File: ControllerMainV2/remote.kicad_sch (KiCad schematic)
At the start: 26 parts, among them IC22 1462039-4, IC23 1462039-4, IC24 1462039-4, IC25 1462039-4, J28 Conn_01x03, J29 Conn_01x03, J31 Conn_01x03, Q1 2N7002, Q2 2N7002, Q3 2N7002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

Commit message: Added libs
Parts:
- removed J28, J29, J31: Conn_01x03, symbol Connector_Generic:Conn_01x03
- removed J30: (no value), symbol Connector_Generic:Conn_01x03

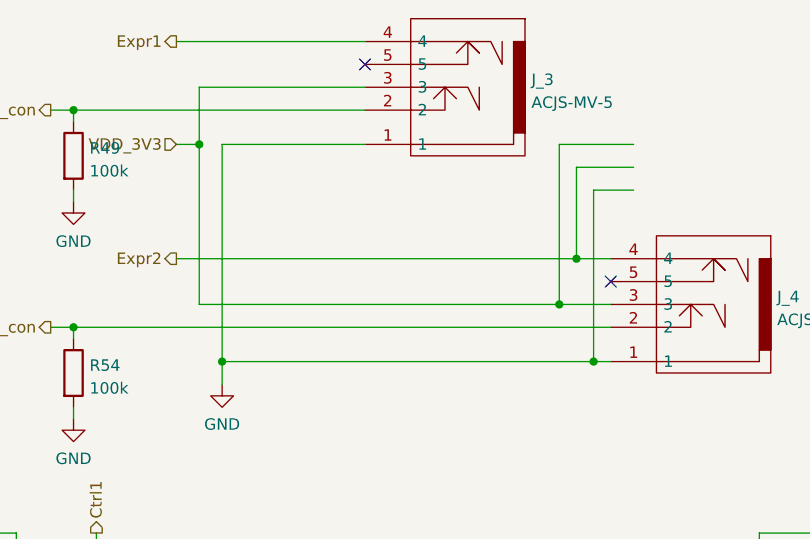
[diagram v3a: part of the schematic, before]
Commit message: 3D models and fixed pcbs
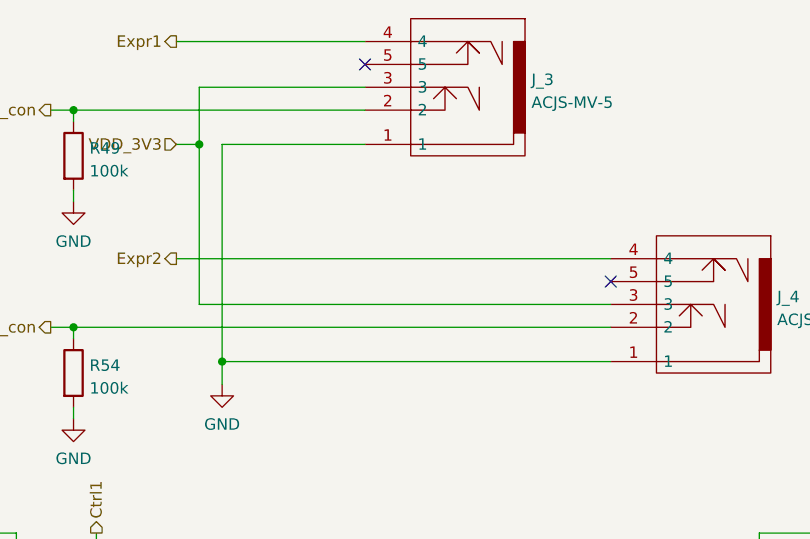
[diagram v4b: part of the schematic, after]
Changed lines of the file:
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@@
   (junction (at 111.76 80.01) (diameter 0) (color 0 0 0 0)
   )
-  (junction (at 167.005 58.42) (diameter 0) (color 0 0 0 0)
-  )
   (junction (at 102.87 130.81) (diameter 0) (color 0 0 0 0)
   )
@@
   (junction (at 123.19 34.29) (diameter 0) (color 0 0 0 0)
   )
-  (junction (at 163.195 52.07) (diameter 0) (color 0 0 0 0)
-  )
   (junction (at 240.03 90.17) (diameter 0) (color 0 0 0 0)
-  )
-  (junction (at 165.1 46.99) (diameter 0) (color 0 0 0 0)
   )
   (junction (at 175.26 90.17) (diameter 0) (color 0 0 0 0)
@@
     (stroke (width 0) (type default) (color 0 0 0 0))
   )
-  (wire (pts (xy 123.19 52.07) (xy 163.195 52.07))
+  (wire (pts (xy 123.19 52.07) (xy 168.91 52.07))
     (stroke (width 0) (type default) (color 0 0 0 0))
   )
@@
     (stroke (width 0) (type default) (color 0 0 0 0))
   )
-  (wire (pts (xy 163.195 52.07) (xy 168.91 52.07))
-    (stroke (width 0) (type default) (color 0 0 0 0))
-  )
   (wire (pts (xy 185.42 109.22) (xy 247.65 109.22))
     (stroke (width 0) (type default) (color 0 0 0 0))
@@
     (stroke (width 0) (type default) (color 0 0 0 0))
   )
-  (wire (pts (xy 171.45 34.29) (xy 163.195 34.29))
-    (stroke (width 0) (type default) (color 0 0 0 0))
-  )
   (wire (pts (xy 67.31 95.25) (xy 67.31 109.22))
     (stroke (width 0) (type default) (color 0 0 0 0))
   )
-  (wire (pts (xy 165.1 36.83) (xy 165.1 46.99))
-    (stroke (width 0) (type default) (color 0 0 0 0))
-  )
   (wire (pts (xy 175.26 90.17) (xy 175.26 130.81))
     (stroke (width 0) (type default) (color 0 0 0 0))
@@
     (stroke (width 0) (type default) (color 0 0 0 0))
   )
-  (wire (pts (xy 171.45 36.83) (xy 165.1 36.83))
-    (stroke (width 0) (type default) (color 0 0 0 0))
-  )
   (wire (pts (xy 186.69 97.79) (xy 184.15 97.79))
     (stroke (width 0) (type default) (color 0 0 0 0))
@@
     (stroke (width 0) (type default) (color 0 0 0 0))
   )
-  (wire (pts (xy 165.1 46.99) (xy 168.91 46.99))
+  (wire (pts (xy 120.65 46.99) (xy 168.91 46.99))
     (stroke (width 0) (type default) (color 0 0 0 0))
   )
@@
     (stroke (width 0) (type default) (color 0 0 0 0))
   )
-  (wire (pts (xy 120.65 46.99) (xy 165.1 46.99))
-    (stroke (width 0) (type default) (color 0 0 0 0))
-  )
   (wire (pts (xy 111.76 120.65) (xy 121.92 120.65))
     (stroke (width 0) (type default) (color 0 0 0 0))
@@
     (stroke (width 0) (type default) (color 0 0 0 0))
   )
-  (wire (pts (xy 171.45 39.37) (xy 167.005 39.37))
-    (stroke (width 0) (type default) (color 0 0 0 0))
-  )
   (wire (pts (xy 121.92 120.65) (xy 121.92 121.92))
     (stroke (width 0) (type default) (color 0 0 0 0))
@@
     (stroke (width 0) (type default) (color 0 0 0 0))
   )
-  (wire (pts (xy 167.005 39.37) (xy 167.005 58.42))
-    (stroke (width 0) (type default) (color 0 0 0 0))
-  )
   (wire (pts (xy 121.92 80.01) (xy 121.92 81.28))
     (stroke (width 0) (type default) (color 0 0 0 0))
@@
     (stroke (width 0) (type default) (color 0 0 0 0))
   )
-  (wire (pts (xy 163.195 34.29) (xy 163.195 52.07))
-    (stroke (width 0) (type default) (color 0 0 0 0))
-  )
-  (wire (pts (xy 167.005 58.42) (xy 168.91 58.42))
+  (wire (pts (xy 125.73 58.42) (xy 168.91 58.42))
     (stroke (width 0) (type default) (color 0 0 0 0))
   )
@@
     (stroke (width 0) (type default) (color 0 0 0 0))
   )
-  (wire (pts (xy 125.73 58.42) (xy 167.005 58.42))
-    (stroke (width 0) (type default) (color 0 0 0 0))
-  )
